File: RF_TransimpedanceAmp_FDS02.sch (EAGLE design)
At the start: 38 parts, among them IC1 PMA-5452, IC2 PMA-5452, IC3 PMA-5452, IC4 ADM7150ARDZ-3.0, IC5 ADM7150ARDZ-5.0, X1 SMAJ502

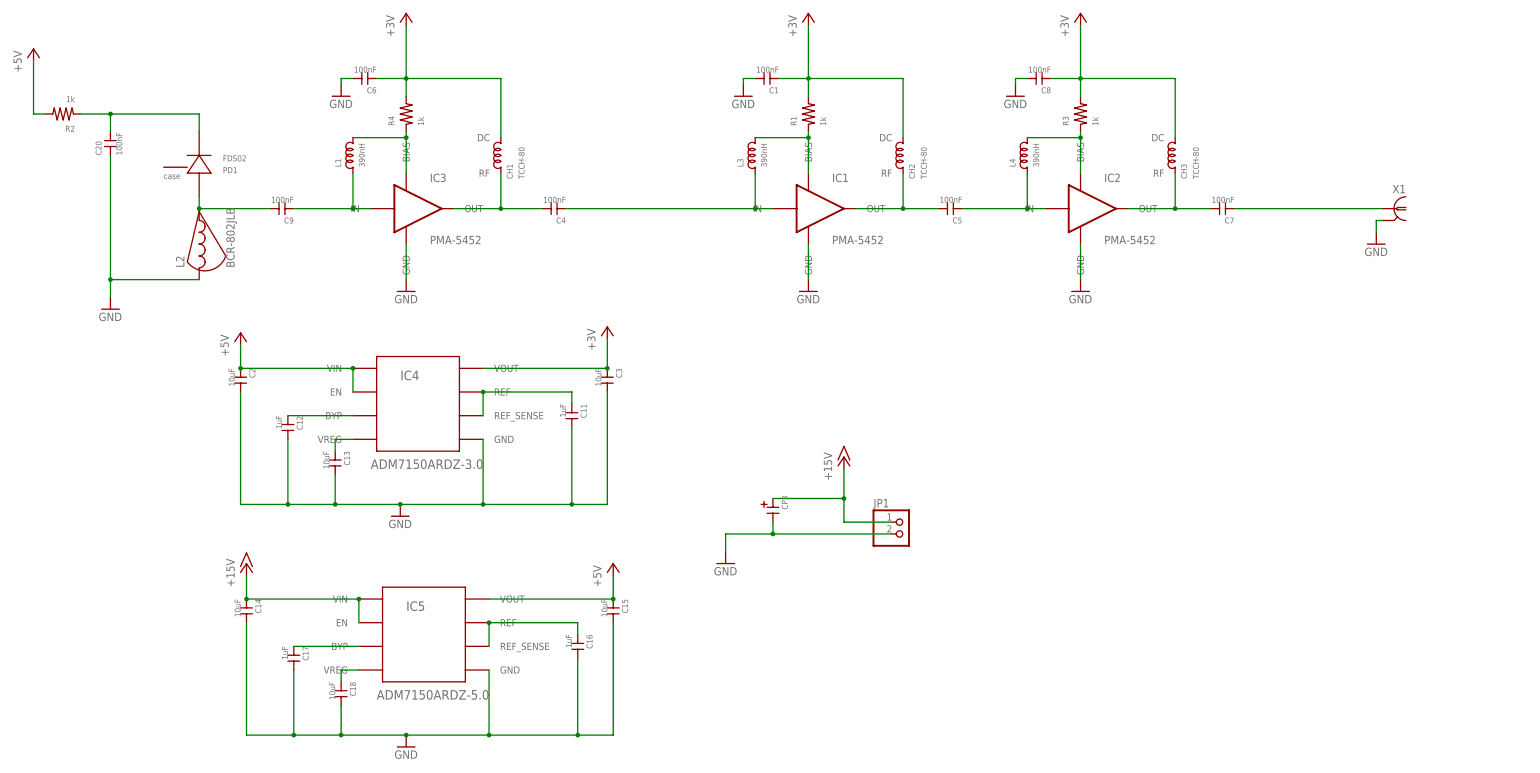
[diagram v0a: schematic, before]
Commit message: Added SMA photodiode input; output monitor
Switch between FDS02 or other photodiode by soldering 0ohm jumper.
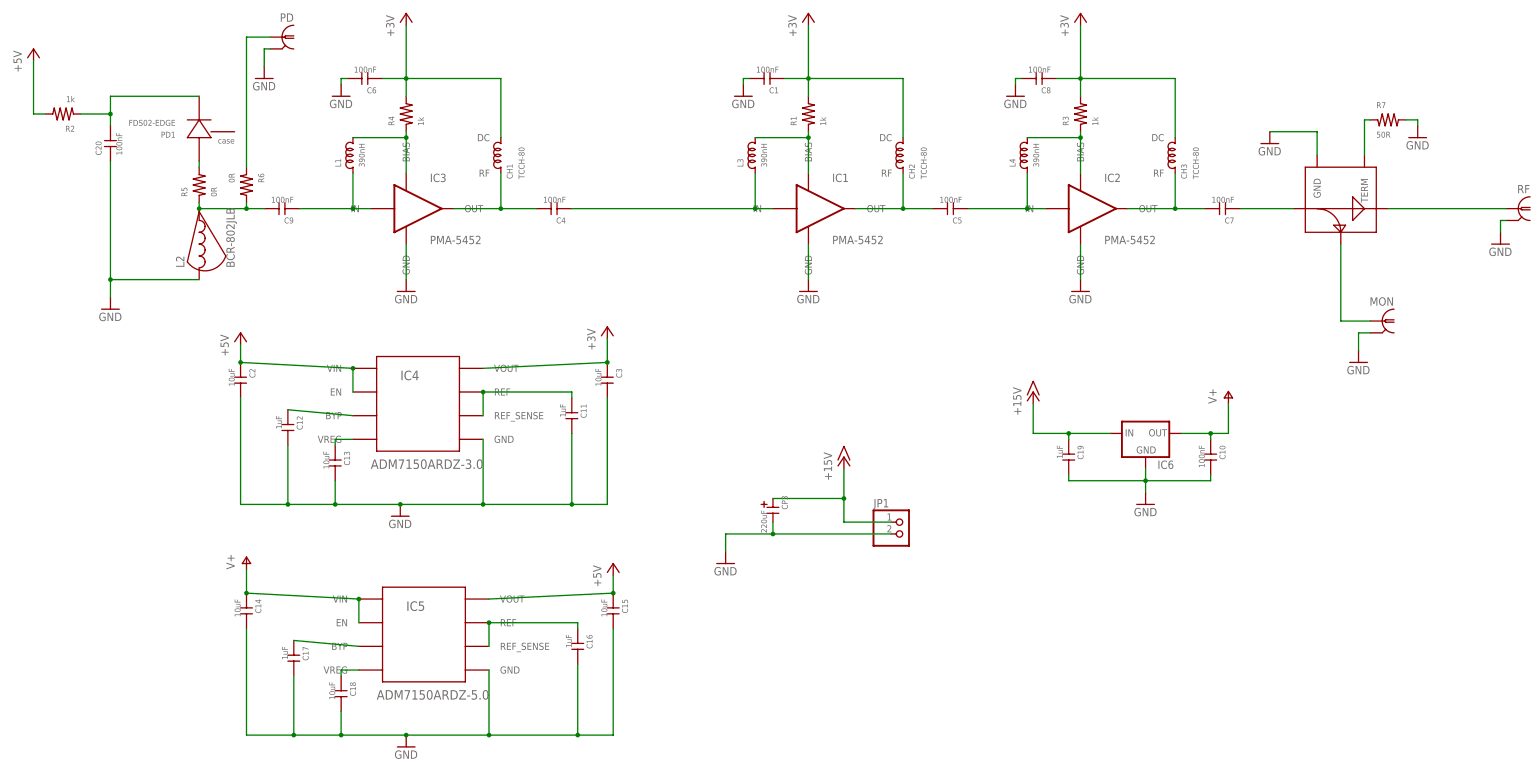
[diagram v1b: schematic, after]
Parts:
- removed X1: SMAJ502, connector-jqi:SMAJ502
- added C10: 100nF, rlc-jqi:CAP0603
- added C19: 1uF, rlc-jqi:CAP0603
- added IC6: (no value), regulator-jqi:78XX-TO220
- added MON, PD: SMAJ502-bulkhead, connector-jqi:SMAJ502
- added R5, R6: 0R, rlc-jqi:RES0402
- added R7: 50R, rlc-jqi:RES0603
- added RF: SMAJ502, connector-jqi:SMAJ502
- added U$1: ADC-10-4, RF_TransimpedanceAmp:ADC-10-4
- C11, C12, C16, C17: device rlc-jqi:CAP0402 -> rlc-jqi:CAP0603
- CP3: value (none) -> 220uF
- PD1: value FDS02 -> FDS02-EDGE; device semiconductor-jqi:FDS02 -> RF_TransimpedanceAmp:FDS02-EDGE
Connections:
- new net N$11: C7.P$1, U$1.IN
- new net N$12: MON.1, U$1.COUP
- new net N$16: PD1.ANODE, R5.P$2
- new net N$17: PD.1, R6.P$1
- new net N$20: R7.P$1, U$1.TERM
- new net V+: C10.P$1, C14.P$1, IC5.EN, IC5.VIN, IC6.OUT
- net +15V: now also C19.P$1, IC6.IN; no longer C14.P$1, IC5.EN, IC5.VIN
- net GND: now also C10.P$2, C19.P$2, IC6.GND, MON.2, PD.2, R7.P$2, RF.2, U$1.GND; no longer X1.2
- net N$4: now also RF.1, U$1.OUT; no longer C7.P$1, X1.1
- net N$7: now also R5.P$1, R6.P$2; no longer PD1.ANODE
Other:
- moved on the sheet: PD1
